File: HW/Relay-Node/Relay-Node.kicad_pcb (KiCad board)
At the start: 2 copper layers, 60 parts, among them IC1 STM8S003F3P, J1 CONN_01X04, J2 CONN_01X04, J3 CONN_01X04, J4 CONN_01X04, M1 NRF24L01, Q1 C1815, Q2 C1815, Q3 C1815, SW1 SW_Push, SW2 SW_Push, U1 ASM1117, U2 MC34063, U3 MAX485

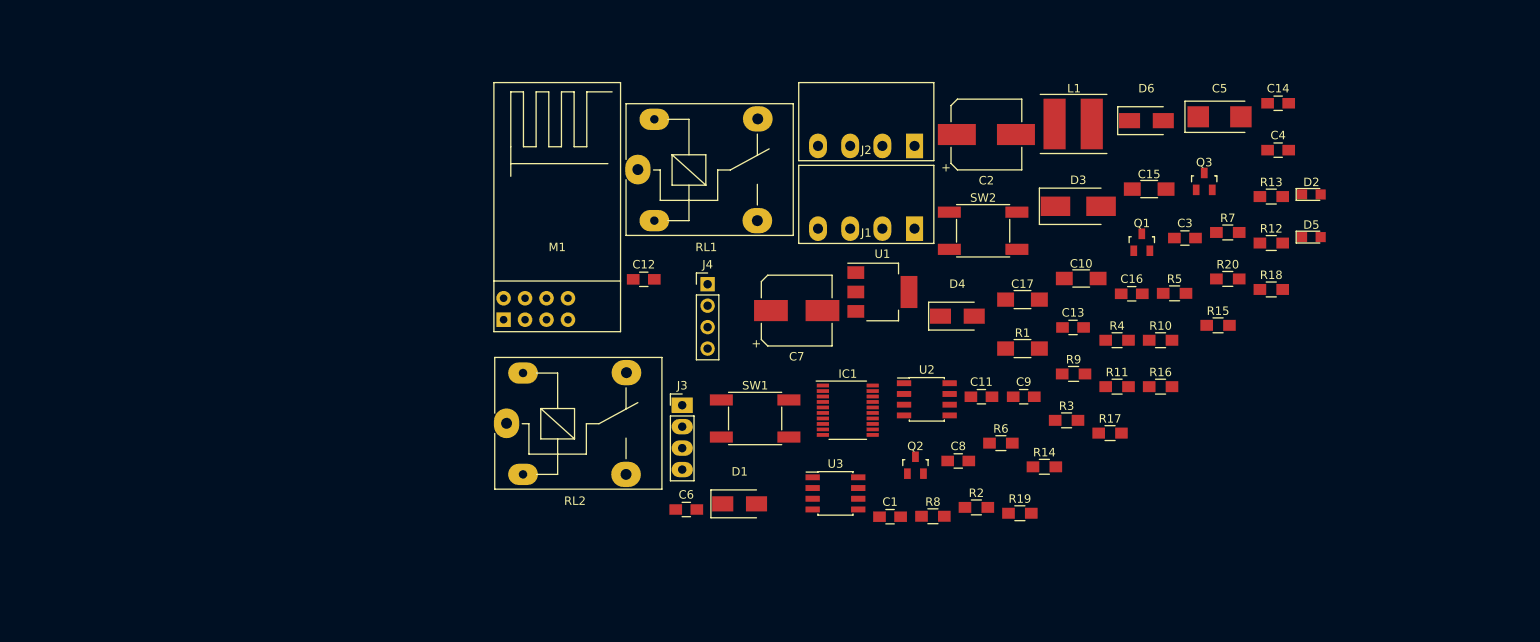
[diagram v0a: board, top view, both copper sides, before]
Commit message: add cover on pcb
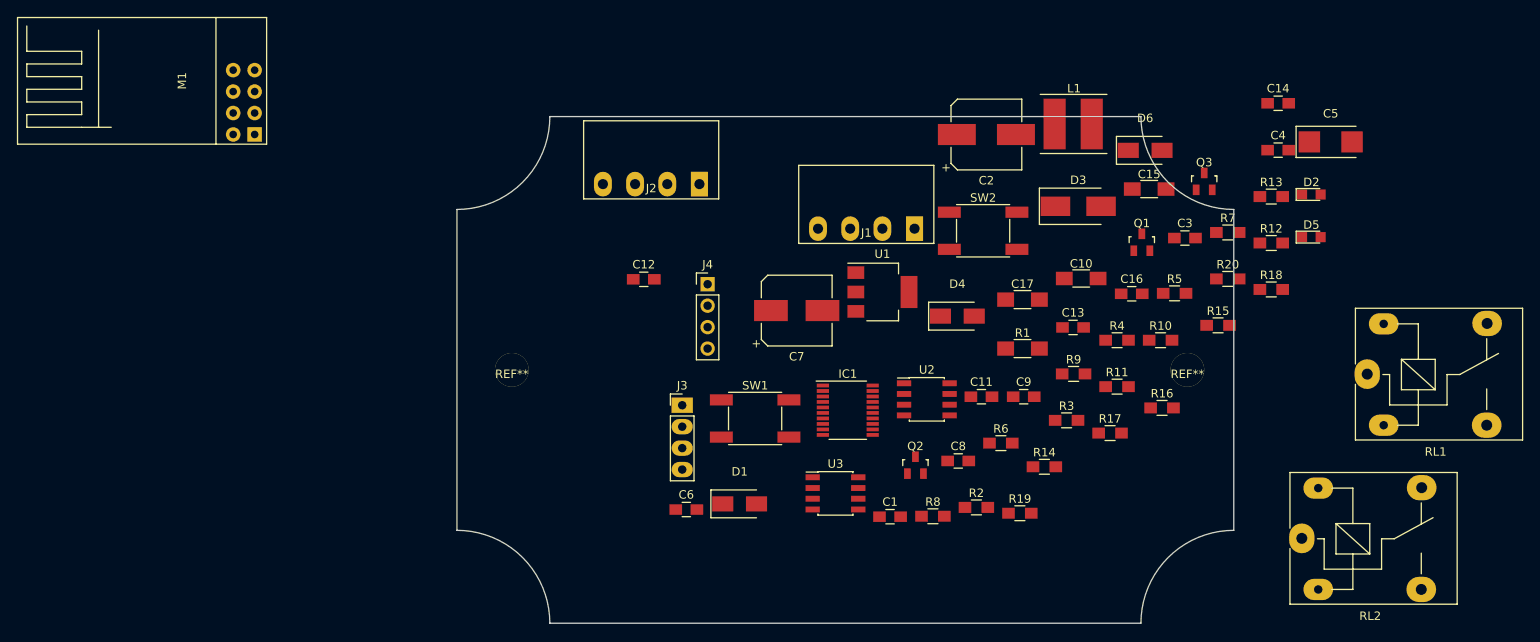
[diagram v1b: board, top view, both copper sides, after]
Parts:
- added REF**: Vit-4mm, nhantt-kicad-lib:Vit-4mm, F.Cu at (176.5, 115.0)
- added REF**: Vit-4mm, nhantt-kicad-lib:Vit-4mm, F.Cu at (96.5, 115.0)
- moved RL2 95.2 mm to (190.1, 134.9)
- moved RL1 89.7 mm to (197.8, 115.5)
- moved M1 47.0 mm to (61.0, 80.8), turned to 90 degrees
- moved J2 25.9 mm to (113.0, 93.0)
- moved C5 13.5 mm to (193.5, 88.0)
- moved D6 3.52 mm to (171.5, 89.0)
- moved R16 2.52 mm to (173.5, 119.5)
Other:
- board outline added: 92 x 60 mm
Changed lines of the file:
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@@
 (kicad_pcb (version 4) (host pcbnew 4.0.6)
   (general
-    (links 135)
+    (links 0)
     (no_connects 135)
-    (area 150.1 104.7 249.360002 160.24)
+    (area 89.924999 84.924999 182.075001 145.075001)
     (thickness 1.6)
-    (drawings 0)
+    (drawings 8)
     (tracks 0)
     (zones 0)
-    (modules 60)
+    (modules 62)
     (nets 45)
   )
@@
     (pad_to_mask_clearance 0.2)
     (aux_axis_origin 0 0)
+    (grid_origin 90 145)
     (visible_elements 7FFFFFFF)
     (pcbplotparams
@@
     (add_net VIN)
   )
+  (module nhantt-kicad-lib:Vit-4mm locked (layer F.Cu)
+    (at 176.5 115)
+    (fp_text reference REF** (at 0 0.5) (layer F.SilkS)
+      (effects (font (size 1 1) (thickness 0.15)))
+    )
+    (fp_text value Vit-4mm (at 0 -0.5) (layer F.Fab)
+      (effects (font (size 1 1) (thickness 0.15)))
+    )
+    (pad 1 thru_hole circle (at 0 0) (size 4 4) (drill 4) (layers *.Cu *.Mask F.SilkS))
+  )
   (module Capacitors_SMD:C_0805_HandSoldering (layer F.Cu)
     (at 141.289524 132.385)
@@
   )
   (module Capacitors_Tantalum_SMD:CP_Tantalum_Case-C_EIA-6032-28_Reflow (layer F.Cu)
-    (at 180.315001 85.025)
+    (at 193.475 88)
     (descr "Tantalum capacitor, Case C, EIA 6032-28, 6.0x3.2x2.5mm, Reflow soldering footprint")
     (tags "capacitor tantalum smd")
@@
   )
   (module nhantt-kicad-lib:D_SMA_Standard (layer F.Cu)
-    (at 171.64762 85.485)
+    (at 171.5 89)
     (descr "Diode SMA")
     (tags "Diode SMA")
@@
   )
   (module nhantt-kicad-lib:Terminal-3.81-4pin (layer F.Cu)
-    (at 138.475001 88.475001)
+    (at 113 93)
     (fp_text reference J2 (at 0 0.5) (layer F.SilkS)
       (effects (font (size 1 1) (thickness 0.15)))
@@
   )
   (module nhantt-kicad-lib:NRF24L01 (layer F.Cu)
-    (at 101.875001 103.975001)
-    (fp_text reference M1 (at 0 -3.5) (layer F.SilkS)
-      (effects (font (size 1 1) (thickness 0.15)))
-    )
-    (fp_text value NRF24L01 (at 0 -6.5) (layer F.Fab)
+    (at 60.96 80.77 90)
+    (fp_text reference M1 (at 0 -3.5 90) (layer F.SilkS)
+      (effects (font (size 1 1) (thickness 0.15)))
+    )
+    (fp_text value NRF24L01 (at 0 -6.5 90) (layer F.Fab)
       (effects (font (size 1 1) (thickness 0.15)))
     )
@@
     (fp_line (start -7.5 6.5) (end -7.5 -23) (layer F.SilkS) (width 0.15))
     (fp_line (start -7.5 6.5) (end 7.5 6.5) (layer F.SilkS) (width 0.15))
-    (pad 1 thru_hole rect (at -6.35 5.08) (size 1.724 1.724) (drill 0.9) (layers *.Cu *.Mask)
-      (net 2 GND))
-    (pad 2 thru_hole circle (at -6.35 2.54) (size 1.724 1.724) (drill 0.9) (layers *.Cu *.Mask)
+    (pad 1 thru_hole rect (at -6.35 5.08 90) (size 1.724 1.724) (drill 0.9) (layers *.Cu *.Mask)
+      (net 2 GND))
+    (pad 2 thru_hole circle (at -6.35 2.54 90) (size 1.724 1.724) (drill 0.9) (layers *.Cu *.Mask)
       (net 3 +3V3))
-    (pad 3 thru_hole circle (at -3.81 5.08) (size 1.724 1.724) (drill 0.9) (layers *.Cu *.Mask)
+    (pad 3 thru_hole circle (at -3.81 5.08 90) (size 1.724 1.724) (drill 0.9) (layers *.Cu *.Mask)
       (net 25 /CE))
-    (pad 4 thru_hole circle (at -3.81 2.54) (size 1.724 1.724) (drill 0.9) (layers *.Cu *.Mask)
+    (pad 4 thru_hole circle (at -3.81 2.54 90) (size 1.724 1.724) (drill 0.9) (layers *.Cu *.Mask)
       (net 26 /CSN))
-    (pad 5 thru_hole circle (at -1.27 5.08) (size 1.724 1.724) (drill 0.9) (layers *.Cu *.Mask)
+    (pad 5 thru_hole circle (at -1.27 5.08 90) (size 1.724 1.724) (drill 0.9) (layers *.Cu *.Mask)
       (net 27 /SCK))
-    (pad 6 thru_hole circle (at -1.27 2.54) (size 1.724 1.724) (drill 0.9) (layers *.Cu *.Mask)
+    (pad 6 thru_hole circle (at -1.27 2.54 90) (size 1.724 1.724) (drill 0.9) (layers *.Cu *.Mask)
       (net 28 /MOSI))
-    (pad 7 thru_hole circle (at 1.27 5.08) (size 1.724 1.724) (drill 0.9) (layers *.Cu *.Mask)
+    (pad 7 thru_hole circle (at 1.27 5.08 90) (size 1.724 1.724) (drill 0.9) (layers *.Cu *.Mask)
       (net 29 /MISO))
-    (pad 8 thru_hole circle (at 1.27 2.54) (size 1.724 1.724) (drill 0.9) (layers *.Cu *.Mask)
+    (pad 8 thru_hole circle (at 1.27 2.54 90) (size 1.724 1.724) (drill 0.9) (layers *.Cu *.Mask)
       (net 30 /IRQ))
     (model E:/Project/2017/hw/kicad/nhantt-kicad-lib/packages3d/NRF24L01P.wrl
@@
   )
   (module Resistors_SMD:R_0805_HandSoldering (layer F.Cu)
-    (at 173.325001 116.985)
+    (at 173.5 119.5)
     (descr "Resistor SMD 0805, hand soldering")
     (tags "resistor 0805")
@@
   )
   (module nhantt-kicad-lib:Relay_SRD-SONGLE (layer F.Cu)
-    (at 111.425001 91.275)
+    (at 197.8 115.5)
     (descr "relay Sanyou SRD series Form C http://www.sanyourelay.ca/public/products/pdf/SRD.pdf")
     (tags "relay Sanyu SRD form C")
@@
   )
   (module nhantt-kicad-lib:Relay_SRD-SONGLE (layer F.Cu)
-    (at 95.875001 121.325)
+    (at 190.05 134.95)
     (descr "relay Sanyou SRD series Form C http://www.sanyourelay.ca/public/products/pdf/SRD.pdf")
     (tags "relay Sanyu SRD form C")
@@
     )
   )
+  (module nhantt-kicad-lib:Vit-4mm locked (layer F.Cu)
+    (at 96.5 115)
+    (fp_text reference REF** (at 0 0.5) (layer F.SilkS)
+      (effects (font (size 1 1) (thickness 0.15)))
+    )
+    (fp_text value Vit-4mm (at 0 -0.5) (layer F.Fab)
+      (effects (font (size 1 1) (thickness 0.15)))
+    )
+    (pad 1 thru_hole circle (at 0 0) (size 4 4) (drill 4) (layers *.Cu *.Mask F.SilkS))
+  )
+  (gr_arc (start 182 85) (end 182 96) (angle 90) (layer Edge.Cuts) (width 0.15))
+  (gr_arc (start 182 145) (end 171 145) (angle 90) (layer Edge.Cuts) (width 0.15))
+  (gr_arc (start 90 85) (end 101 85) (angle 90) (layer Edge.Cuts) (width 0.15))
+  (gr_arc (start 90 145) (end 90 134) (angle 90) (layer Edge.Cuts) (width 0.15))
+  (gr_line (start 182 96) (end 182 134) (layer Edge.Cuts) (width 0.15))
+  (gr_line (start 90 96) (end 90 134) (layer Edge.Cuts) (width 0.15))
+  (gr_line (start 101 85) (end 171 85) (layer Edge.Cuts) (width 0.15))
+  (gr_line (start 101 145) (end 171 145) (layer Edge.Cuts) (width 0.15))
 )

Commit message: layout pcb relay-node
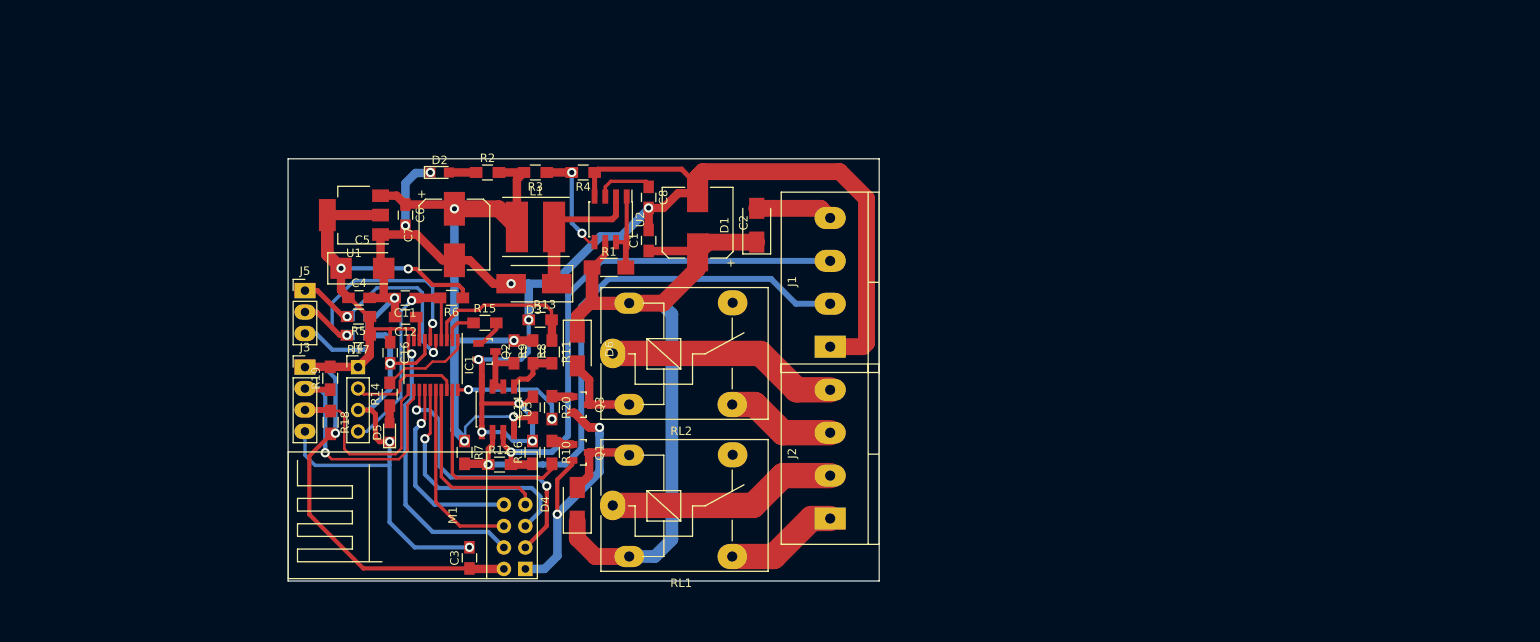
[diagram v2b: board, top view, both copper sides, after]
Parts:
- removed C10, C15: 100nF, Capacitors_SMD:C_1206_HandSoldering
- removed C17: 10uF, Resistors_SMD:R_1206_HandSoldering
- removed REF** (x2): Vit-4mm, nhantt-kicad-lib:Vit-4mm
- removed SW1, SW2: SW_Push, nhantt-kicad-lib:Button-6mm-smd
- added J5: CONN_01X03, nhantt-kicad-lib:Header-3pin-2.54, F.Cu at (72.0, 105.6)
- C13, C9: moved to B.Cu
- J1, J2: footprint nhantt-kicad-lib:Terminal-3.81-4pin -> nhantt-kicad-lib:Domino-5.08mm_4pol
- RL1, RL2: value G5Q-1 -> FINDER-40.51
- moved C5 115.6 mm to (78.8, 103.0)
- moved R18 112.5 mm to (75.0, 121.2), turned to 270 degrees
- moved D5 111.6 mm to (82.0, 122.4), turned to 90 degrees
- moved C4 110.2 mm to (78.4, 106.5)
- moved D2 103.3 mm to (88.0, 91.6)
- moved R5 96.7 mm to (78.3, 108.7), turned to 180 degrees
- moved C14 95.3 mm to (99.0, 119.4), turned to 90 degrees
- moved R12 95.1 mm to (95.0, 126.2)
- moved R7 94.1 mm to (90.9, 124.8), turned to 270 degrees
- moved C3 92.8 mm to (91.5, 137.3), turned to 90 degrees
- moved RL1 90.7 mm to (108.5, 131.1)
- moved R17 89.8 mm to (78.3, 110.9), turned to 180 degrees
- moved C16 88.1 mm to (82.1, 113.0), turned to 270 degrees
- moved R13 87.8 mm to (99.8, 109.1), turned to 180 degrees
- moved R15 86.8 mm to (93.3, 109.4)
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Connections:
- D4 pad 2: Net-(C10-Pad2) -> Net-(D4-Pad2)
- D6 pad 2: Net-(C15-Pad2) -> Net-(D6-Pad2)
- J1 pad 1: VIN -> GND
- J1 pad 4: GND -> VIN
- Q1 pad 3: Net-(C10-Pad2) -> Net-(D4-Pad2)
- Q3 pad 3: Net-(C15-Pad2) -> Net-(D6-Pad2)
- R17 pad 1: +5V -> +3V3
- R2 pad 2: +3V3 -> +5V
- R5 pad 1: +5V -> +3V3
- RL1 pad 1: Net-(C10-Pad2) -> Net-(J2-Pad2)
- RL1 pad 2: Net-(J2-Pad2) -> +12V
- RL1 pad 5: +12V -> Net-(D4-Pad2)
- RL2 pad 1: Net-(C15-Pad2) -> Net-(J2-Pad4)
- RL2 pad 2: Net-(J2-Pad4) -> Net-(D6-Pad2)
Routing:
- net GND: track 0.00 -> 284.5 mm, vias 0 -> 15
- net +3V3: track 0.00 -> 106.1 mm, vias 0 -> 3
- net +12V: track 0.00 -> 91.6 mm
- net +5V: track 0.00 -> 76.9 mm, vias 0 -> 4
- net /A: track 0.00 -> 67.6 mm, vias 0 -> 1
- net /B: track 0.00 -> 63.8 mm, vias 0 -> 1
- net /CSN: track 0.00 -> 34.1 mm, vias 0 -> 1
- net /CE: track 0.00 -> 33.2 mm, vias 0 -> 2
- net /button2: track 0.00 -> 30.9 mm, vias 0 -> 2
- net /SCL: track 0.00 -> 30.6 mm, vias 0 -> 1
- net /SCK: track 0.00 -> 29.3 mm, vias 0 -> 1
- net Net-(J2-Pad4): track 0.00 -> 27.5 mm
- net /NRST: track 0.00 -> 27.3 mm, vias 0 -> 1
- net Net-(J2-Pad2): track 0.00 -> 27.2 mm
- net /button1: track 0.00 -> 26.0 mm, vias 0 -> 2
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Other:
- board size 92 x 60 mm -> 70 x 50 mm
- net class Default: trace_width 0.25 -> 0.3; via_dia 0.6 -> 1.1; via_drill 0.4 -> 0.6

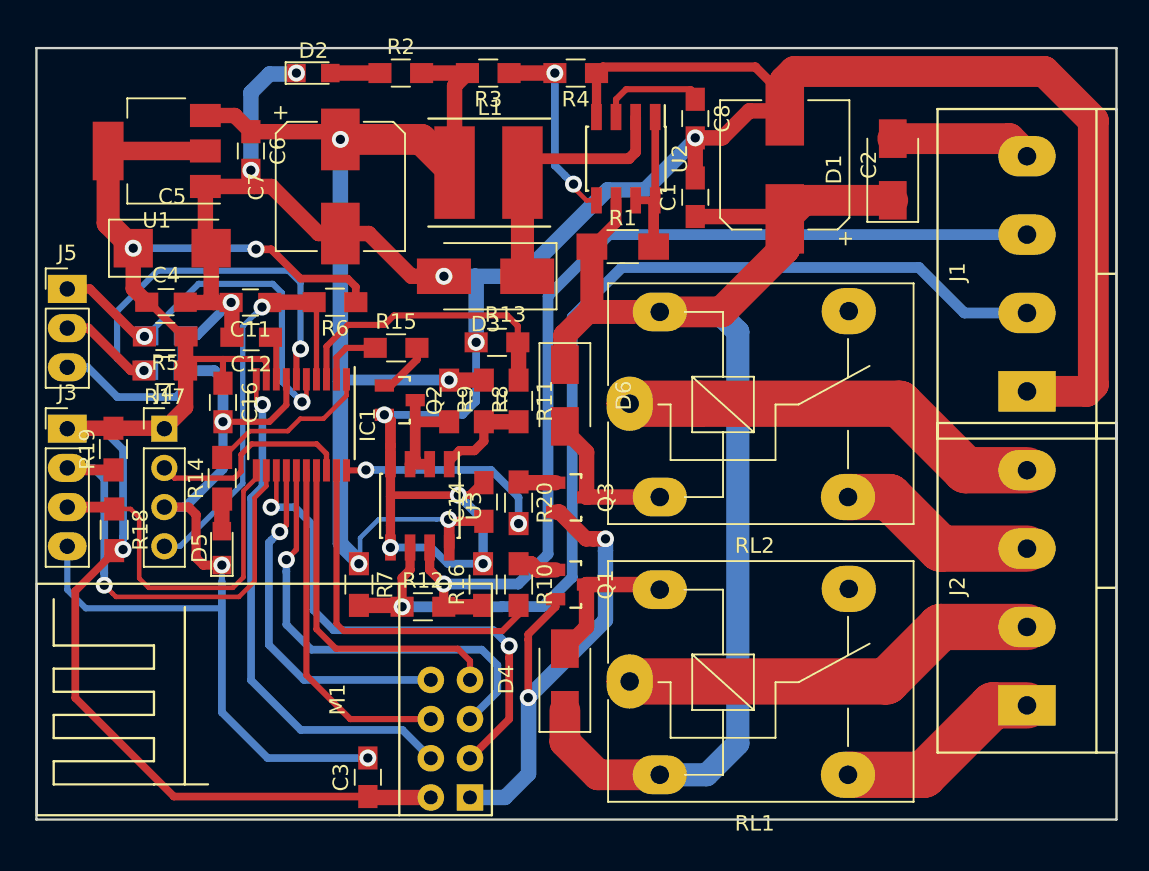
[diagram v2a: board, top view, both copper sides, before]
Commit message: add vit-hole
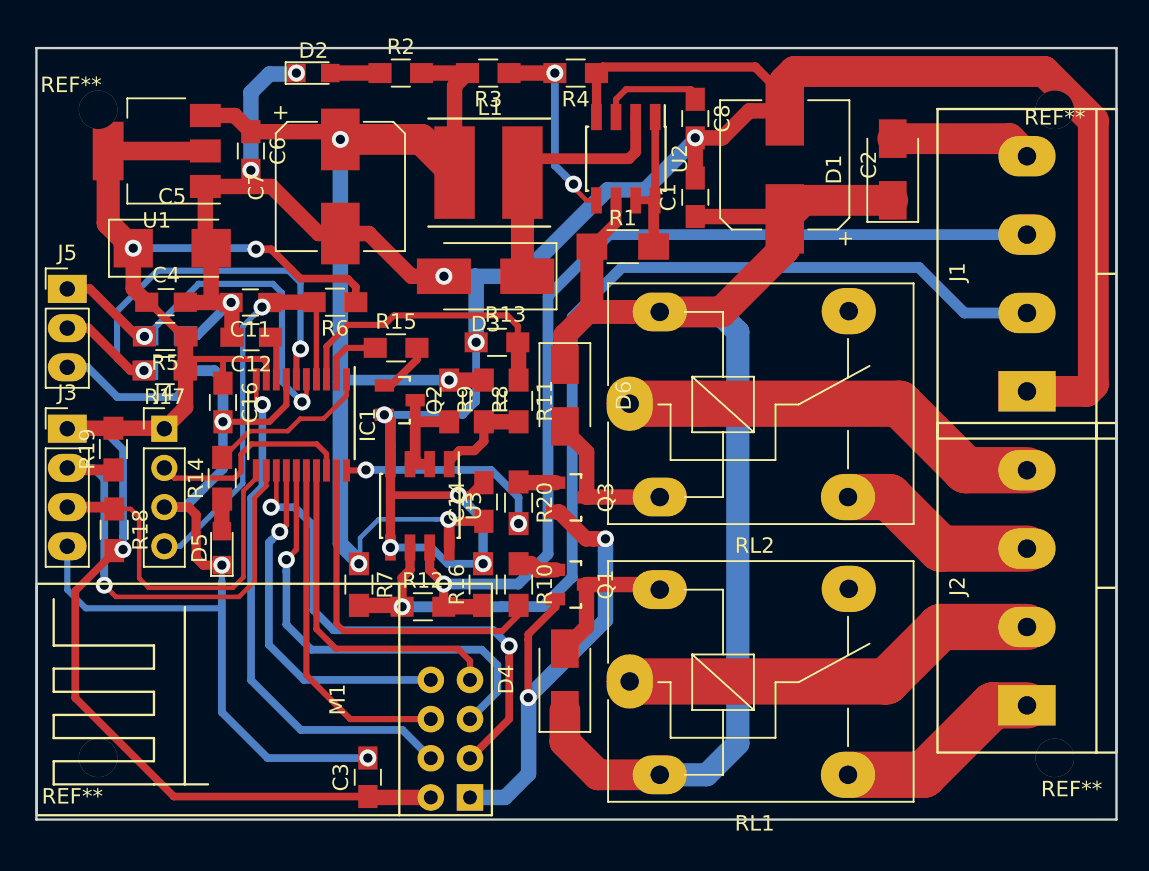
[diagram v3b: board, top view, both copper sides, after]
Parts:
- added REF**: Vit-4mm, nhantt-kicad-lib:Vit-3mm, F.Cu at (72.3, 138.0)
- added REF**: Vit-4mm, nhantt-kicad-lib:Vit-3mm, F.Cu at (136.0, 94.0)
- added REF**: Vit-4mm, nhantt-kicad-lib:Vit-3mm, F.Cu at (137.1, 137.5)
- added REF**: Vit-4mm, nhantt-kicad-lib:Vit-3mm, F.Cu at (72.2, 91.9)
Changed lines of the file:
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@@
 (kicad_pcb (version 4) (host pcbnew 4.0.6)
   (general
-    (links 124)
-    (no_connects 35)
-    (area 69.924999 89.924999 140.075001 140.075001)
+    (links 0)
+    (no_connects 1)
+    (area 68.659048 88.895 141.275 141.325)
     (thickness 1.6)
     (drawings 4)
     (tracks 500)
     (zones 0)
-    (modules 56)
+    (modules 60)
     (nets 45)
   )
@@
     (mod_text_size 1 1)
     (mod_text_width 0.15)
-    (pad_size 1.524 1.524)
-    (pad_drill 0.762)
+    (pad_size 2.5 2.5)
+    (pad_drill 2.5)
     (pad_to_mask_clearance 0.2)
     (aux_axis_origin 0 0)
@@
     (add_net VIN)
   )
+  (module nhantt-kicad-lib:Vit-3mm (layer F.Cu)
+    (at 72.33 138)
+    (fp_text reference REF** (at 0 0.5) (layer F.SilkS)
+      (effects (font (size 1 1) (thickness 0.15)))
+    )
+    (fp_text value Vit-4mm (at 0 -0.5) (layer F.Fab)
+      (effects (font (size 1 1) (thickness 0.15)))
+    )
+    (pad 1 thru_hole circle (at 1.67 -2) (size 2.5 2.5) (drill 2.5) (layers *.Cu *.Mask F.SilkS))
+  )
+  (module nhantt-kicad-lib:Vit-3mm (layer F.Cu)
+    (at 136 94)
+    (fp_text reference REF** (at 0 0.5) (layer F.SilkS)
+      (effects (font (size 1 1) (thickness 0.15)))
+    )
+    (fp_text value Vit-4mm (at 0 -0.5) (layer F.Fab)
+      (effects (font (size 1 1) (thickness 0.15)))
+    )
+    (pad 1 thru_hole circle (at 0 0) (size 2.5 2.5) (drill 2.5) (layers *.Cu *.Mask F.SilkS))
+  )
+  (module nhantt-kicad-lib:Vit-3mm (layer F.Cu)
+    (at 137.09 137.53)
+    (fp_text reference REF** (at 0 0.5) (layer F.SilkS)
+      (effects (font (size 1 1) (thickness 0.15)))
+    )
+    (fp_text value Vit-4mm (at 0 -0.5) (layer F.Fab)
+      (effects (font (size 1 1) (thickness 0.15)))
+    )
+    (pad 1 thru_hole circle (at -1.09 -1.53) (size 2.5 2.5) (drill 2.5) (layers *.Cu *.Mask F.SilkS))
+  )
   (module Capacitors_SMD:C_0805_HandSoldering (layer F.Cu)
     (at 112.7 99.67 90)
@@
     )
   )
+  (module nhantt-kicad-lib:Vit-3mm (layer F.Cu)
+    (at 72.24 91.89)
+    (fp_text reference REF** (at 0 0.5) (layer F.SilkS)
+      (effects (font (size 1 1) (thickness 0.15)))
+    )
+    (fp_text value Vit-4mm (at 0 -0.5) (layer F.Fab)
+      (effects (font (size 1 1) (thickness 0.15)))
+    )
+    (pad 1 thru_hole circle (at 1.76 2.11) (size 2.5 2.5) (drill 2.5) (layers *.Cu *.Mask F.SilkS))
+  )
   (gr_line (start 70 90) (end 70 140) (layer Edge.Cuts) (width 0.15))
